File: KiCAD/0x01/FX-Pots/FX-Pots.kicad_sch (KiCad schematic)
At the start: 28 parts, among them J1 Conn_01x05, J2 Conn_01x05, SW1 SW_Push_LED, SW2 SW_Push_LED, SW3 SW_Push_LED, SW4 SW_Push_LED, U1 74HC595, U2 CD74HC4067M

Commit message: fx-pots
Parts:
- removed J1, J2: Conn_01x05, Connector_PinSocket_2.54mm:PinSocket_1x05_P2.54mm_Vertical, symbol Connector_Generic:Conn_01x05
- removed U1: 74HC595, Package_SO:SOIC-16_3.9x9.9mm_P1.27mm, symbol 74xx:74HC595
- removed U2: CD74HC4067M, Package_SO:SOIC-24W_7.5x15.4mm_P1.27mm, symbol 74xx:CD74HC4067M
- added C1, C2: 10uF, Capacitor_SMD:C_0805_2012Metric_Pad1.18x1.45mm_HandSolder, symbol Device:C_Small
- added C10, C11, C8, C9: 1uF, Capacitor_SMD:C_1206_3216Metric_Pad1.33x1.80mm_HandSolder, symbol Device:C_Small
- added J1: IN, Connector_JST:JST_PH_S4B-PH-K_1x04_P2.00mm_Horizontal, symbol Connector_Generic:Conn_01x04
- added J2: OUT, Connector_JST:JST_PH_S4B-PH-K_1x04_P2.00mm_Horizontal, symbol Connector_Generic:Conn_01x04
- added JP1, JP3: A0, Jumper:SolderJumper-2_P1.3mm_Open_RoundedPad1.0x1.5mm, symbol Jumper:SolderJumper_2_Open
- added JP2, JP4: A1, Jumper:SolderJumper-2_P1.3mm_Open_RoundedPad1.0x1.5mm, symbol Jumper:SolderJumper_2_Open
- added R1, R2: 10K, Capacitor_SMD:C_0805_2012Metric_Pad1.18x1.45mm_HandSolder, symbol Device:R_Small
- added R11, R12, R13, R14: 220, PCM_Resistor_SMD_AKL:R_1206_3216Metric_Pad1.30x1.75mm_HandSolder, symbol Device:R_Small
- added R15, R16, R17, R18: 10K, PCM_Resistor_SMD_AKL:R_1206_3216Metric_Pad1.30x1.75mm_HandSolder, symbol Device:R_Small
- added RN1: R_Pack04_10K, Resistor_SMD:R_Array_Convex_4x0603, symbol Device:R_Pack04
- added RV5, RV6, RV7, RV8: R_Pot, Potentiometer_THT:Potentiometer_Bourns_PTV09A-1_Single_Vertical, symbol Device:R_Potentiometer_Small
- added SW5, SW6, SW7, SW8: SW_Push_LED, led-switch:SW_PUSH_6mm_LED, symbol Switch:SW_Push_LED
- added U1, U2: ADS7830, Package_SO:TSSOP-16_4.4x5mm_P0.65mm, symbol Analog_DAC:ADS7830
- SW1, SW2, SW3, SW4: footprint led-sw:led switch -> led-switch:SW_PUSH_6mm_LED
- renumbered C1 to C4, C2 to C5, C3 to C6, C4 to C7, R8 to R10, R1 to R3, R2 to R4, R3 to R5, R4 to R6, R5 to R7, R6 to R8, R7 to R9
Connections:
- net +5V: now also C1.1, C2.1, J1.2 (Pin_2), J2.3 (Pin_3), R1.1, R15.1, R16.1, R17.1, R18.1, R2.1, RV5.1, RV6.1, RV7.1, RV8.1, U1.16 (VDD), U2.16 (VDD)
- net FXSW1: now also U1.2 (CH1)
- net FXSW2: now also U1.4 (CH3)
- net FXSW3: now also U1.6 (CH5)
- net FXSW4: now also U1.8 (CH7)
- net GND: now also C1.2, C10.2, C11.2, C2.2, C8.2, C9.2, J1.1 (Pin_1), J2.4 (Pin_4), R11.1, R12.1, R13.1, R14.1, RN1.1 (R1.1), RN1.2 (R2.1), RN1.3 (R3.1), RN1.4 (R4.1), RV5.3, RV6.3, RV7.3, RV8.3, SW5.1, SW6.1, SW7.1, SW8.1, U1.9 (GND), U2.9 (GND)
- net POT1: now also U1.1 (CH0)
- net POT2: now also U1.3 (CH2)
- net POT3: now also U1.5 (CH4)
- net POT4: now also U1.7 (CH6)
- new net: R14.2, SW8.3 (K)
- new net: R12.2, SW6.3 (K)
- new net: R13.2, SW7.3 (K)
- new net: JP4.2 (B), RN1.5 (R4.2)
- new net: JP2.2 (B), RN1.7 (R2.2)
- new net: R11.2, SW5.3 (K)
- new net: JP3.2 (B), RN1.6 (R3.2)
- new net: JP1.2 (B), RN1.8 (R1.2)
- new net A0: JP1.1 (A), U1.12 (A0)
- new net A1: JP2.1 (A), U1.13 (A1)
- new net A3: JP3.1 (A), U2.12 (A0)
- new net A4: JP4.1 (A), U2.13 (A1)
- new net FX-LED-5: SW5.4 (A)
- new net FX-LED-6: SW6.4 (A)
- new net FX-LED-7: SW7.4 (A)
- new net FX-LED-8: SW8.4 (A)
- new net FXSW5: C8.1, R15.2, SW5.2, U2.2 (CH1)
- new net FXSW6: C9.1, R16.2, SW6.2, U2.4 (CH3)
- new net FXSW7: C10.1, R17.2, SW7.2, U2.6 (CH5)
- new net FXSW8: C11.1, R18.2, SW8.2, U2.8 (CH7)
- new net POT5: RV5.2, U2.1 (CH0)
- new net POT6: RV6.2, U2.3 (CH2)
- new net POT7: RV7.2, U2.5 (CH4)
- new net POT8: RV8.2, U2.7 (CH6)
- new net SCL: J1.4 (Pin_4), J2.1 (Pin_1), R2.2, U1.14 (SCL), U2.14 (SCL)
- new net SDA: J1.3 (Pin_3), J2.2 (Pin_2), R1.2, U1.15 (SDA), U2.15 (SDA)
- no-connect marks 13 -> 4
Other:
- moved on the sheet: C4, C5, C6, C7, H1, H2, H3, H4, R10, R3, R4, R5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

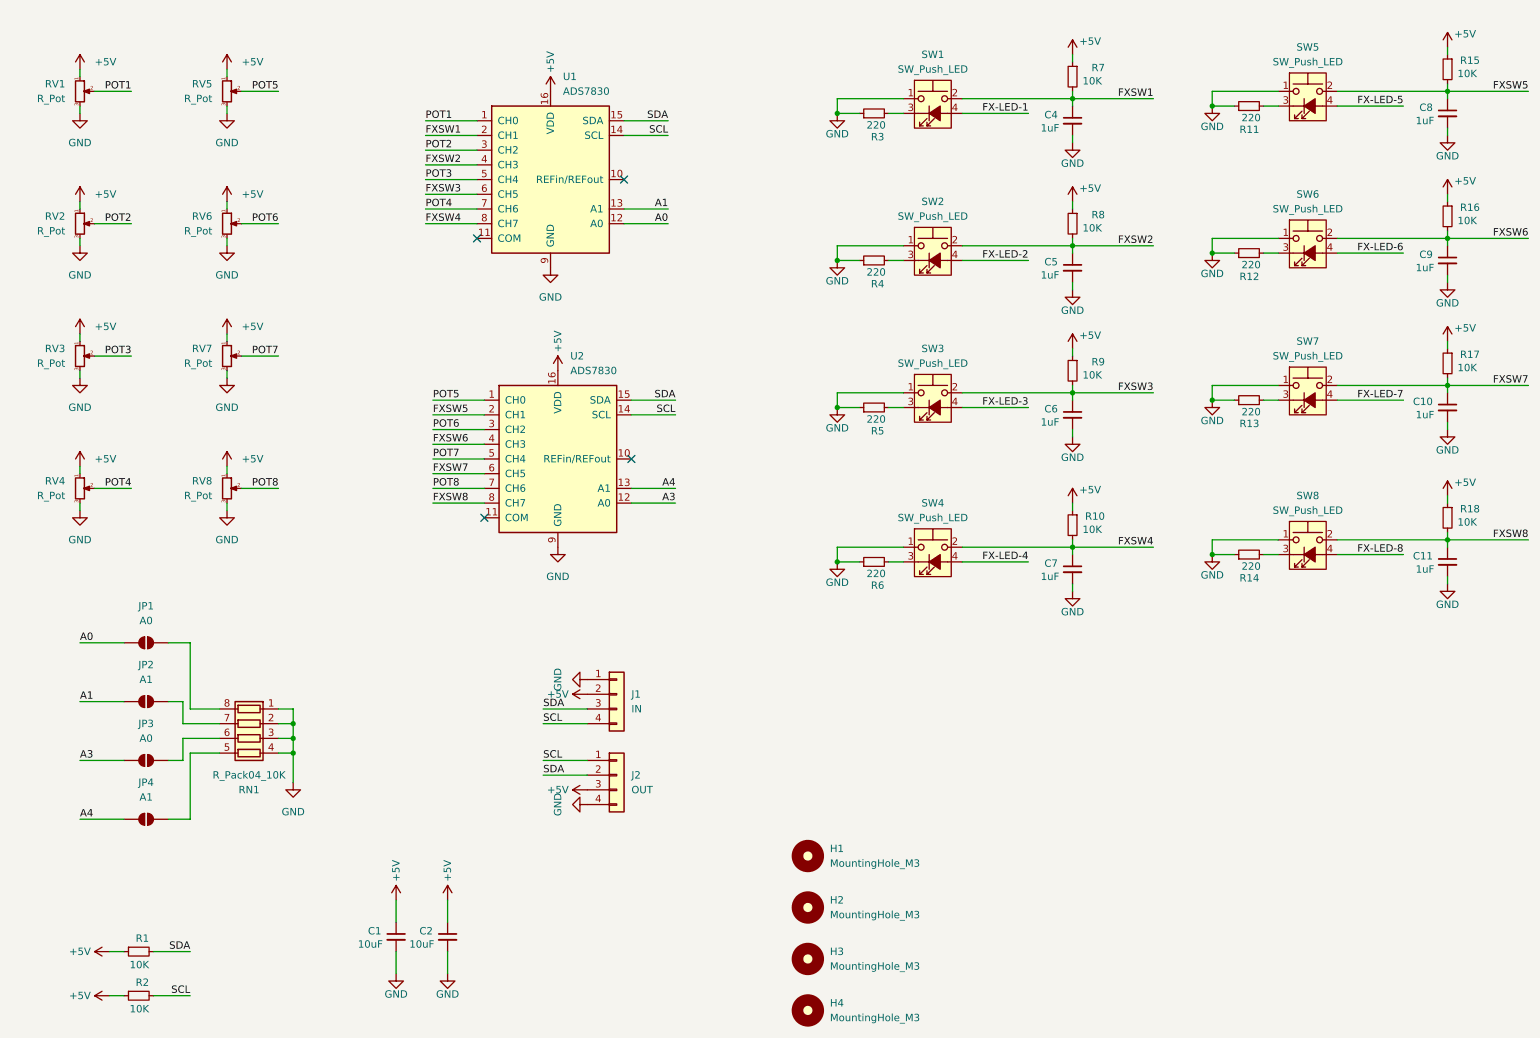
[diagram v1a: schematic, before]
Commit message: pots refactor
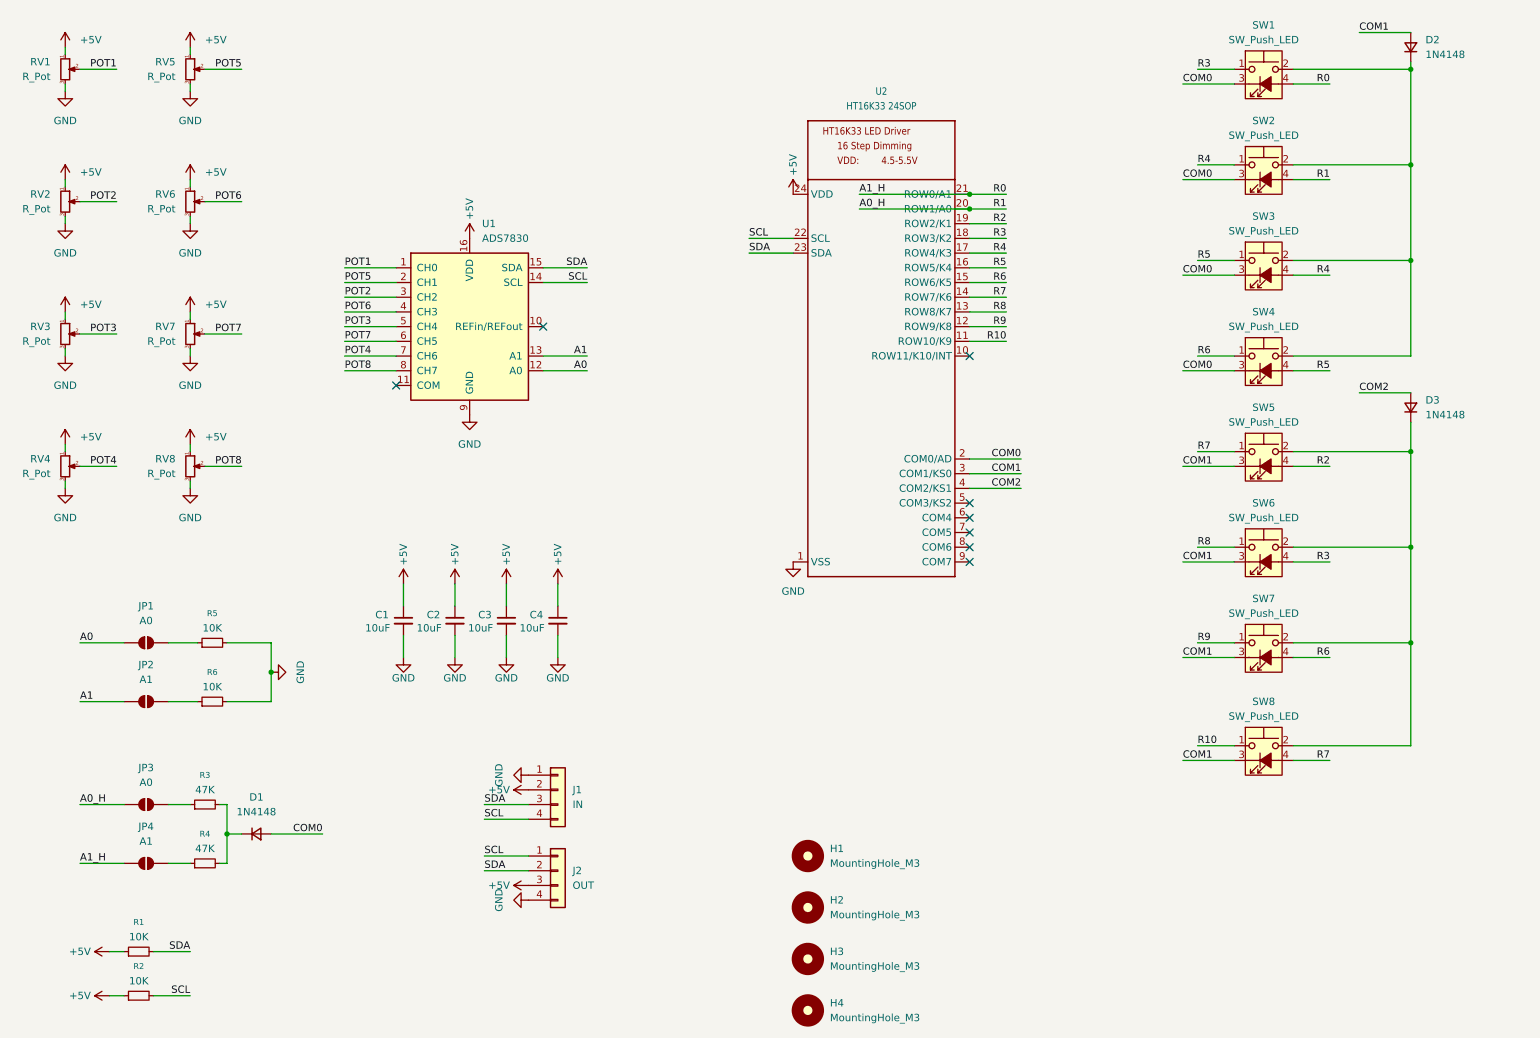
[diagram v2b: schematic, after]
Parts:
- removed C10, C11, C5, C6, C7, C8, C9: 1uF, Capacitor_SMD:C_1206_3216Metric_Pad1.33x1.80mm_HandSolder, symbol Device:C_Small
- removed R10, R15, R16, R17, R18, R7, R8, R9: 10K, PCM_Resistor_SMD_AKL:R_1206_3216Metric_Pad1.30x1.75mm_HandSolder, symbol Device:R_Small
- removed R11, R12, R13, R14: 220, PCM_Resistor_SMD_AKL:R_1206_3216Metric_Pad1.30x1.75mm_HandSolder, symbol Device:R_Small
- removed RN1: R_Pack04_10K, Resistor_SMD:R_Array_Convex_4x0603, symbol Device:R_Pack04
- removed U2: ADS7830, Package_SO:TSSOP-16_4.4x5mm_P0.65mm, symbol Analog_DAC:ADS7830
- added C3: 10uF, Capacitor_SMD:C_0805_2012Metric_Pad1.18x1.45mm_HandSolder, symbol Device:C_Small
- added D1, D2, D3: 1N4148, Diode_SMD:D_SOD-323_HandSoldering, symbol Device:D_Small
- added U2: HT16K33 24SOP, Package_SO:SSOP-24_5.3x8.2mm_P0.65mm, symbol ht16k33_sop28:HT16K33_SOP24
- C4: value 1uF -> 10uF; footprint Capacitor_SMD:C_1206_3216Metric_Pad1.33x1.80mm_HandSolder -> Capacitor_SMD:C_0805_2012Metric_Pad1.18x1.45mm_HandSolder
- R1, R2: footprint Capacitor_SMD:C_0805_2012Metric_Pad1.18x1.45mm_HandSolder -> Resistor_SMD:R_0805_2012Metric_Pad1.20x1.40mm_HandSolder
- R3, R4: value 220 -> 47K; footprint PCM_Resistor_SMD_AKL:R_1206_3216Metric_Pad1.30x1.75mm_HandSolder -> Resistor_SMD:R_0805_2012Metric_Pad1.20x1.40mm_HandSolder
- R5, R6: value 220 -> 10K; footprint PCM_Resistor_SMD_AKL:R_1206_3216Metric_Pad1.30x1.75mm_HandSolder -> Resistor_SMD:R_0805_2012Metric_Pad1.20x1.40mm_HandSolder
- renumbered SW5 to SW3, SW6 to SW4, SW3 to SW5, SW4 to SW6
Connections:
- net FX-LED-1 is gone; now on net A1_H: SW1.4 (A)
- net FX-LED-2 is gone; now on net A0_H: SW2.4 (A)
- net FXSW5 is gone; now on an unnamed net: SW3.2
- net FXSW6 is gone; now on an unnamed net: SW4.2
- net FXSW7 is gone; now on an unnamed net: SW7.2
- net FXSW8 is gone; now on an unnamed net: SW8.2
- net +5V: now also C4.1, C3.1, U2.24 (VDD)
- net GND: now also R5.2, R6.2, C3.2, U2.1 (VSS); no longer R3.1, R4.1, R5.1, R6.1, SW1.1, SW2.1, SW3.1, SW4.1, SW5.1, SW6.1, SW7.1, SW8.1
- net POT5: now also U1.2 (CH1)
- net POT6: now also U1.4 (CH3)
- net POT7: now also U1.6 (CH5)
- net POT8: now also U1.8 (CH7)
- net SCL: now also U2.22 (SCL)
- net SDA: now also U2.23 (SDA)
- net COM1: now reaches SW8.3 (K)
- net COM1: now also SW5.3 (K), SW6.3 (K), SW7.3 (K), D2.2 (A), U2.3 (COM1/KS0)
- net COM0: now reaches SW4.3 (K)
- net COM0: now also SW1.3 (K), SW2.3 (K), SW3.3 (K), D1.2 (A), U2.2 (COM0/AD)
- net at JP4.2 (B): now also R4.1
- net at JP2.2 (B): now also R6.1
- net at JP3.2 (B): now also R3.1
- net at R4.2: now also R3.2, D1.1 (K); no longer SW2.3 (K)
- net at JP1.2 (B): now also R5.1
- net A3 renamed A0_H
- net A0_H: now also U2.20 (ROW1/A0)
- net A4 renamed A1_H
- net A1_H: now also U2.21 (ROW0/A1)
- net FX-LED-3 renamed R2
- net R2: now also U2.19 (ROW2/K1)
- net FX-LED-4 renamed R3
- net R3: now also SW1.1, U2.18 (ROW3/K2)
- net FX-LED-5 renamed R4
- net R4: now also SW2.1, U2.17 (ROW4/K3)
- net FX-LED-6 renamed R5
- net R5: now also SW3.1, U2.16 (ROW5/K4)
- net FX-LED-7 renamed R6
- net R6: now also SW4.1, U2.15 (ROW6/K5)
- net FX-LED-8 renamed R7
- net R7: now also SW5.1, U2.14 (ROW7/K6)
- removed net FXSW1: C4.1, SW1.2, U1.2 (CH1)
- net FXSW2: no longer names the net of SW2.2
- net FXSW2: now also SW1.2, D2.1 (K); no longer U1.4 (CH3)
- net FXSW3: no longer names the net of SW5.2
- net FXSW3: now also SW6.2, D3.1 (K); no longer U1.6 (CH5)
- removed net FXSW4: SW6.2, U1.8 (CH7)
- new net COM2: D3.2 (A), U2.4 (COM2/KS1)
- new net R10: SW8.1, U2.11 (ROW10/K9)
- new net R8: SW6.1, U2.13 (ROW8/K7)
- new net R9: SW7.1, U2.12 (ROW9/K8)
- no-connect marks 4 -> 8
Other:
- moved on the sheet: C1, C2, J1, J2, JP3, JP4, RV1, RV2, RV3, RV4, RV5, RV6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

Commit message: step models
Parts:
- RV1, RV2, RV3, RV4, RV5, RV6, RV7, RV8: footprint Potentiometer_THT:Potentiometer_Bourns_PTV09A-1_Single_Vertical -> led-sw:Potentiometer_Bourns_PTV09A-1_Single_Vertical
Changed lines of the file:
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@@
 			)
 		)
-		(property "Footprint" "Potentiometer_THT:Potentiometer_Bourns_PTV09A-1_Single_Vertical"
+		(property "Footprint" "led-sw:Potentiometer_Bourns_PTV09A-1_Single_Vertical"
 			(at 46.99 73.66 0)
 			(effects
@@
 			)
 		)
-		(property "Footprint" "Potentiometer_THT:Potentiometer_Bourns_PTV09A-1_Single_Vertical"
+		(property "Footprint" "led-sw:Potentiometer_Bourns_PTV09A-1_Single_Vertical"
 			(at 25.4 96.52 0)
 			(effects
@@
 			)
 		)
-		(property "Footprint" "Potentiometer_THT:Potentiometer_Bourns_PTV09A-1_Single_Vertical"
+		(property "Footprint" "led-sw:Potentiometer_Bourns_PTV09A-1_Single_Vertical"
 			(at 25.4 27.94 0)
 			(effects
@@
 			)
 		)
-		(property "Footprint" "Potentiometer_THT:Potentiometer_Bourns_PTV09A-1_Single_Vertical"
+		(property "Footprint" "led-sw:Potentiometer_Bourns_PTV09A-1_Single_Vertical"
 			(at 46.99 50.8 0)
 			(effects
@@
 			)
 		)
-		(property "Footprint" "Potentiometer_THT:Potentiometer_Bourns_PTV09A-1_Single_Vertical"
+		(property "Footprint" "led-sw:Potentiometer_Bourns_PTV09A-1_Single_Vertical"
 			(at 25.4 73.66 0)
 			(effects
@@
 			)
 		)
-		(property "Footprint" "Potentiometer_THT:Potentiometer_Bourns_PTV09A-1_Single_Vertical"
+		(property "Footprint" "led-sw:Potentiometer_Bourns_PTV09A-1_Single_Vertical"
 			(at 46.99 27.94 0)
 			(effects
@@
 			)
 		)
-		(property "Footprint" "Potentiometer_THT:Potentiometer_Bourns_PTV09A-1_Single_Vertical"
+		(property "Footprint" "led-sw:Potentiometer_Bourns_PTV09A-1_Single_Vertical"
 			(at 25.4 50.8 0)
 			(effects
@@
 			)
 		)
-		(property "Footprint" "Potentiometer_THT:Potentiometer_Bourns_PTV09A-1_Single_Vertical"
+		(property "Footprint" "led-sw:Potentiometer_Bourns_PTV09A-1_Single_Vertical"
 			(at 46.99 96.52 0)
 			(effects

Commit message: fixes
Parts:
- U2: footprint Package_SO:SSOP-24_5.3x8.2mm_P0.65mm -> Package_SO:SOIC-24W_7.5x15.4mm_P1.27mm
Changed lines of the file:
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@@
 			)
 		)
-		(property "Footprint" "Package_SO:SSOP-24_5.3x8.2mm_P0.65mm"
+		(property "Footprint" "Package_SO:SOIC-24W_7.5x15.4mm_P1.27mm"
 			(at 166.37 29.972 0)
 			(effects

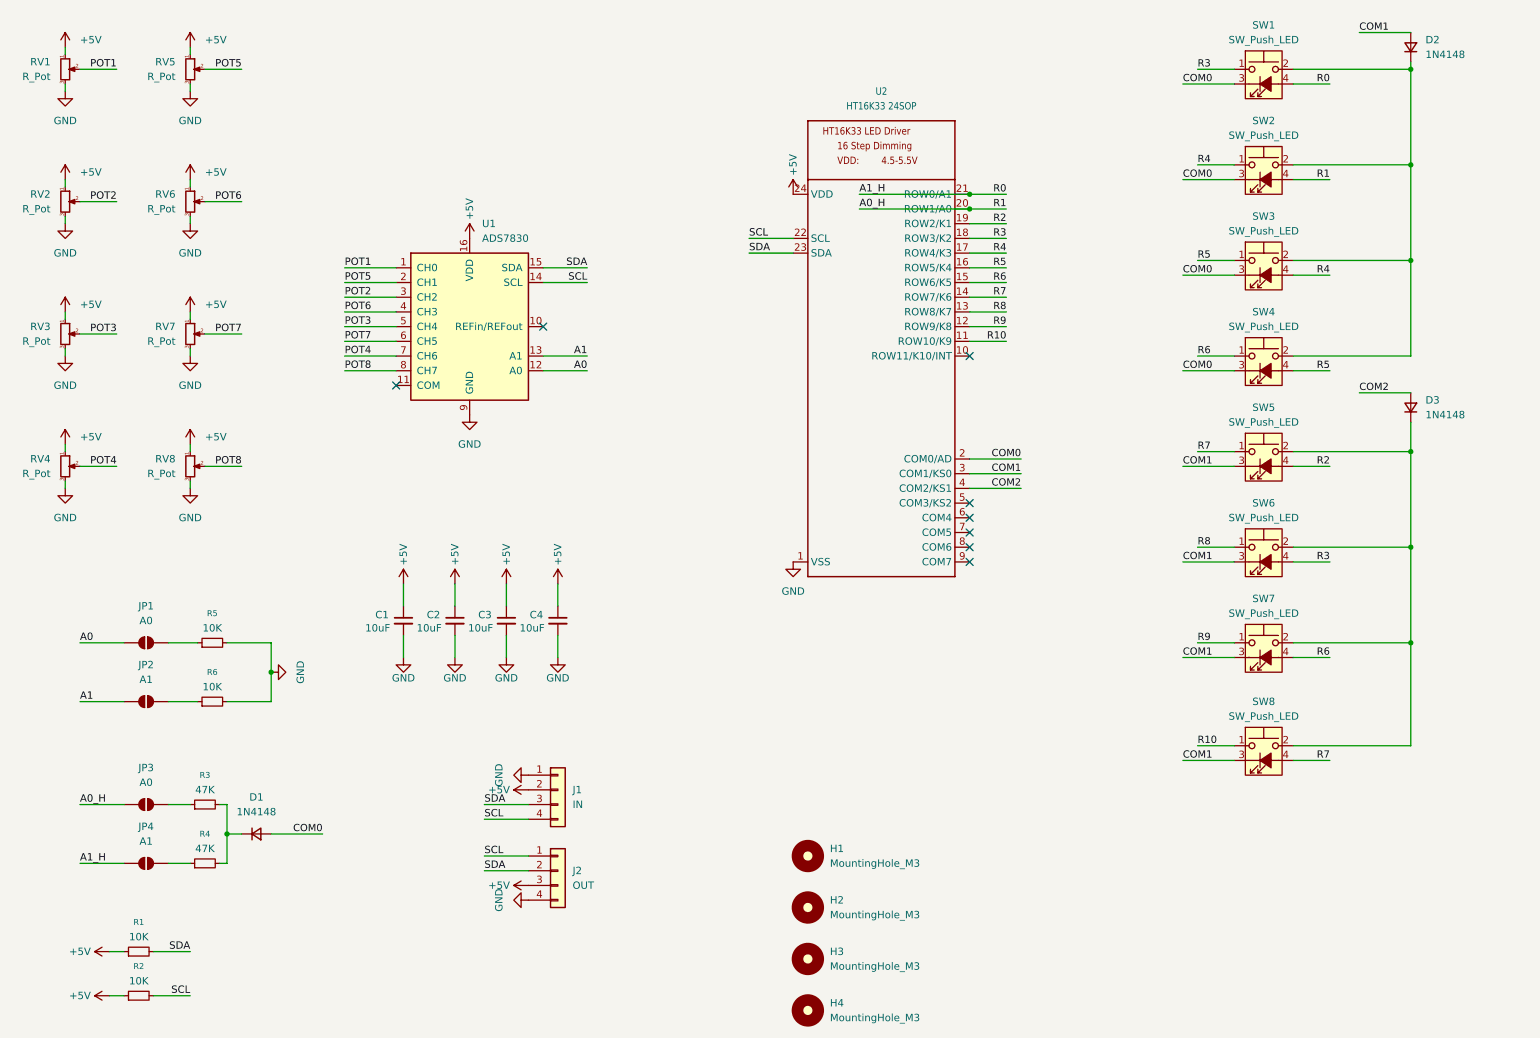
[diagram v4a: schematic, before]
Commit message: fx-pads routing
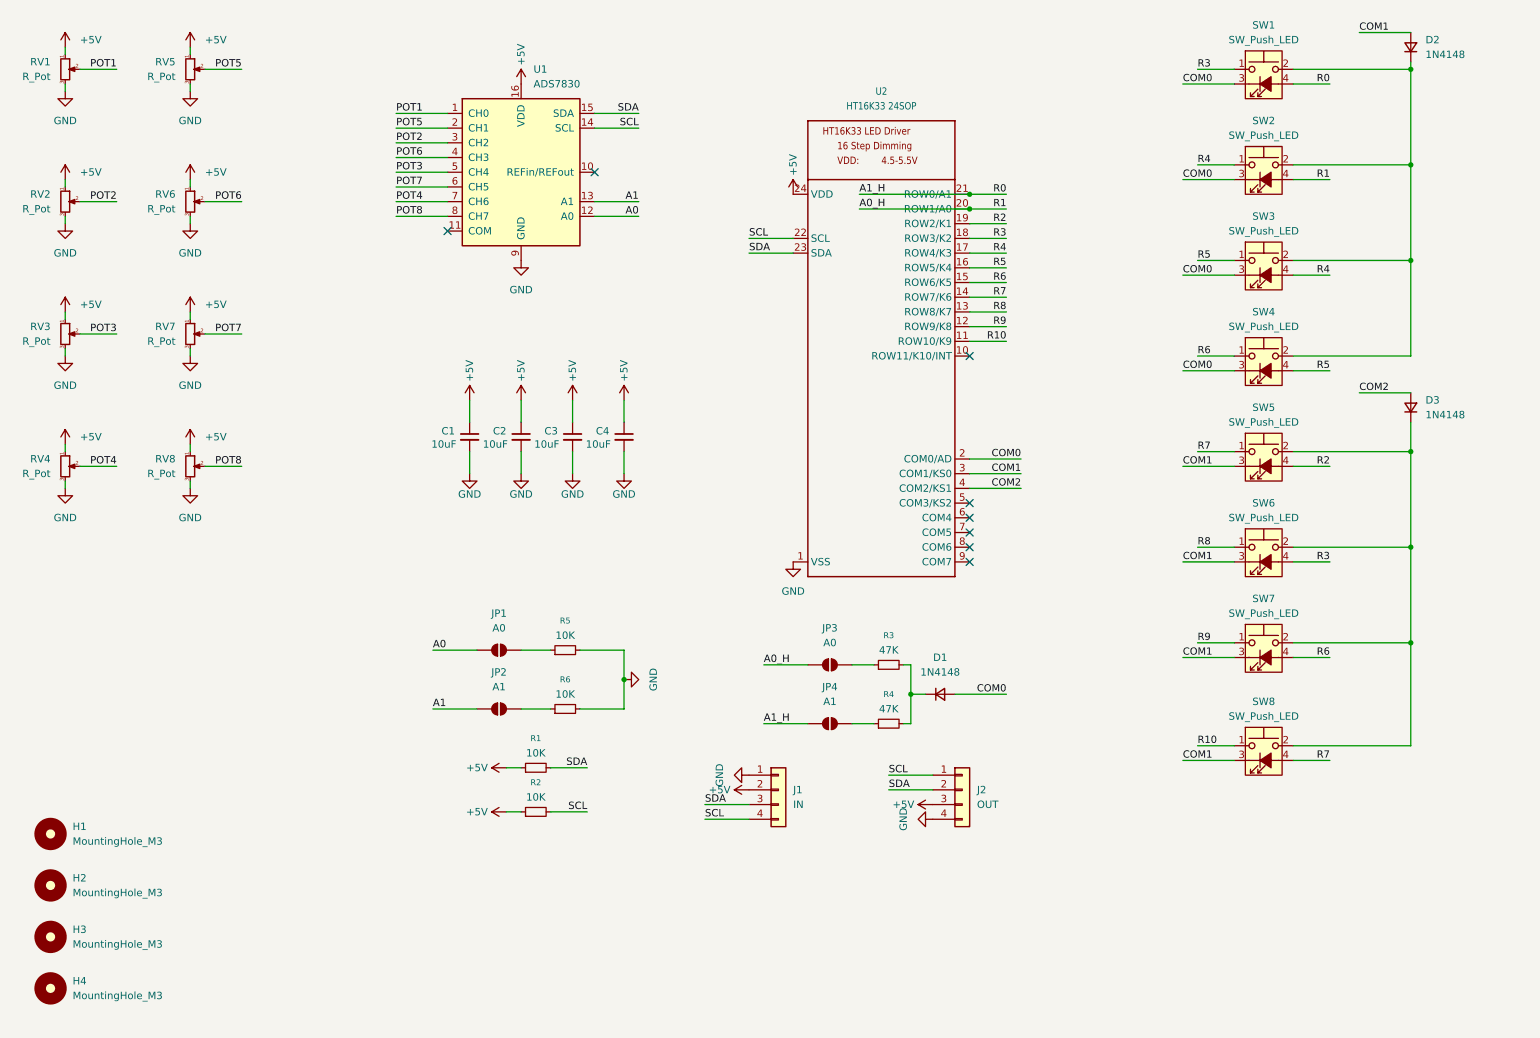
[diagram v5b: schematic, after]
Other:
- moved on the sheet: C1, C2, C3, C4, D1, H1, H2, H3, H4, J1, J2, JP1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
